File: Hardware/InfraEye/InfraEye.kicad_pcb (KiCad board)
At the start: 2 copper layers, 11 parts, among them Q1 Q_NPN_BCE, U1 MLX90640, U2 ESP32-WROOM-32, U3 TFT_SPI_24_LCD, U4 MLX90640

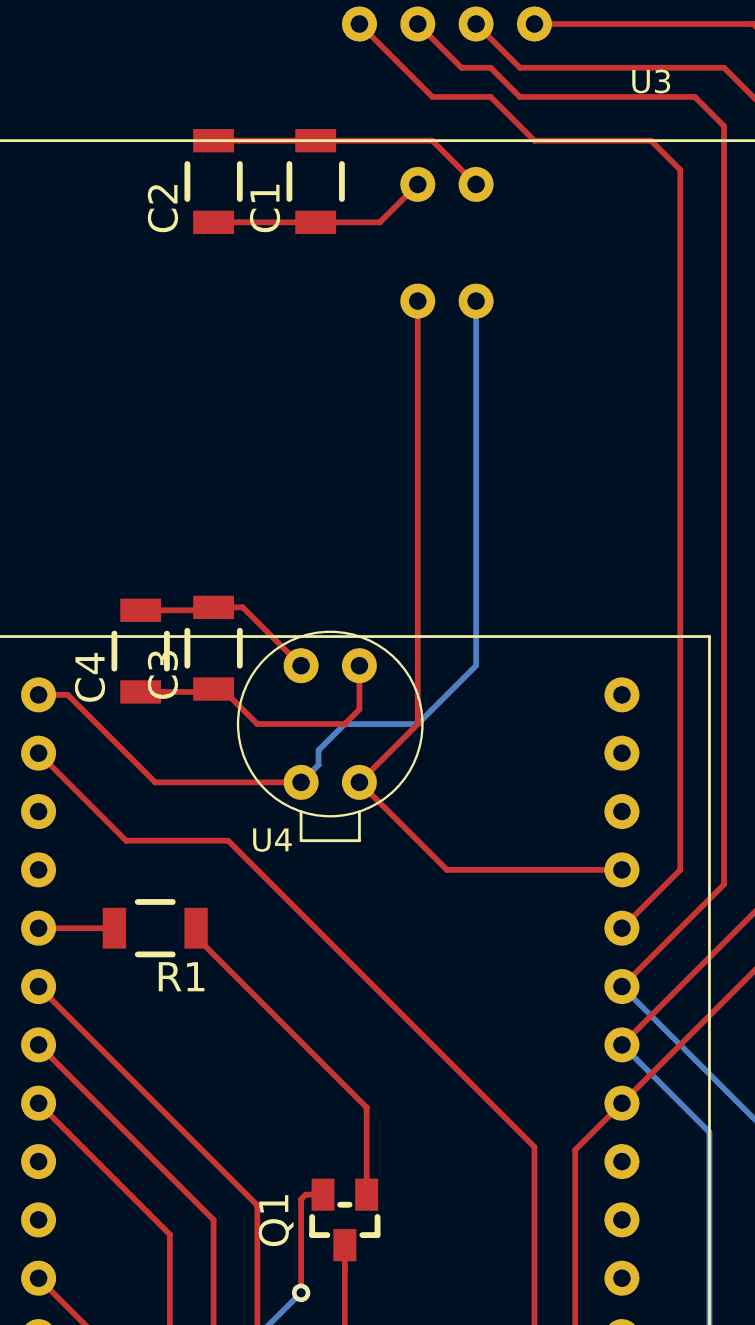
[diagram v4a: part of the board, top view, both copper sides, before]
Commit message: Updated PCB - added text, finished track routing and fill areas. After verifying that it works as it is on schematics, it will be sent out for review.
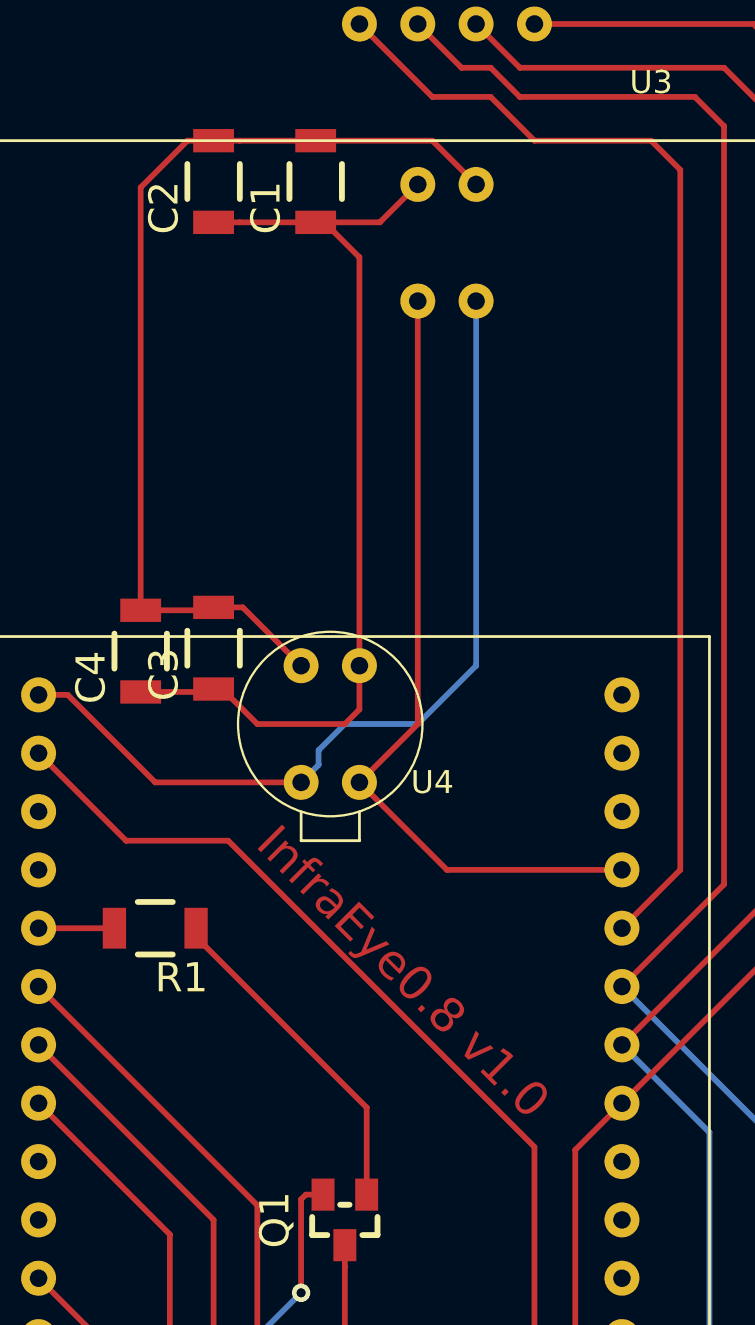
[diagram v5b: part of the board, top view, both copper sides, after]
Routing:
- net GND: track 32.0 -> 54.5 mm
- net +3V3: track 50.6 -> 70.9 mm
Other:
- board text added: "InfraEye0.8 v1.0"
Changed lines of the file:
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@@
   (general
     (thickness 1.6)
-    (drawings 2)
-    (tracks 117)
+    (drawings 3)
+    (tracks 123)
     (zones 0)
     (modules 11)
@@
   (module InfraEye:MLX90614 (layer F.Cu)
     (at 124.46 76.2 180)
-    (fp_text reference U4 (at 3.81 -2.54) (layer F.SilkS)
+    (fp_text reference U4 (at -3.175 0) (layer F.SilkS)
       (effects (font (size 1 1) (thickness 0.15)))
     )
-    (fp_text value MLX90640 (at 1.27 -3.81) (layer F.Fab)
+    (fp_text value MLX90640 (at -4.445 -1.905) (layer F.Fab)
       (effects (font (size 1 1) (thickness 0.15)))
     )
@@
     )
   )
+  (gr_text "InfraEye0.8 v1.0" (at 126.365 84.455 315) (layer F.Cu)
+    (effects (font (size 1.5 1.5) (thickness 0.3)))
+  )
   (gr_line (start 139.7 69.85) (end 139.7 118.11) (layer F.SilkS) (width 0.12))
   (gr_line (start 106.68 69.85) (end 139.7 69.85) (layer F.SilkS) (width 0.12))
-  (via (at 121.92 98.425) (size 0.8) (drill 0.4) (layers F.Cu B.Cu) (net 29))
   (segment (start 128.27 80.01) (end 135.89 80.01) (width 0.25) (layer F.Cu) (net 1))
   (segment (start 124.46 76.2) (end 128.27 80.01) (width 0.25) (layer F.Cu) (net 1))
@@
   (segment (start 127.635 48.26) (end 129.54 50.165) (width 0.25) (layer F.Cu) (net 2))
   (segment (start 122.555 48.26) (end 127.635 48.26) (width 0.25) (layer F.Cu) (net 2))
+  (segment (start 116.971 48.26) (end 114.935 50.296) (width 0.25) (layer F.Cu) (net 2))
+  (segment (start 118.11 48.26) (end 116.971 48.26) (width 0.25) (layer F.Cu) (net 2))
+  (segment (start 114.935 50.296) (end 114.935 68.707) (width 0.25) (layer F.Cu) (net 2))
   (segment (start 121.92 76.2) (end 115.57 76.2) (width 0.25) (layer F.Cu) (net 3))
   (segment (start 111.76 72.39) (end 110.49 72.39) (width 0.25) (layer F.Cu) (net 3))
@@
   (segment (start 116.205 95.885) (end 110.49 90.17) (width 0.25) (layer F.Cu) (net 28))
   (segment (start 116.205 107.315) (end 116.205 95.885) (width 0.25) (layer F.Cu) (net 28))
+  (via (at 121.92 98.425) (size 0.8) (drill 0.4) (layers F.Cu B.Cu) (net 29))
   (segment (start 117.983 72.263) (end 118.11 72.136) (width 0.25) (layer F.Cu) (net 29))
   (segment (start 114.935 72.263) (end 117.983 72.263) (width 0.25) (layer F.Cu) (net 29))
@@
   (segment (start 110.49 107.95) (end 112.395 107.95) (width 0.25) (layer B.Cu) (net 29))
   (segment (start 112.395 107.95) (end 121.92 98.425) (width 0.25) (layer B.Cu) (net 29))
+  (segment (start 122.936 51.816) (end 122.555 51.816) (width 0.25) (layer F.Cu) (net 29))
+  (segment (start 124.46 53.34) (end 122.936 51.816) (width 0.25) (layer F.Cu) (net 29))
+  (segment (start 124.46 71.12) (end 124.46 53.34) (width 0.25) (layer F.Cu) (net 29))
   (segment (start 129.54 114.49237) (end 129.54 115.57) (width 0.25) (layer F.Cu) (net 30))
   (segment (start 129.54 109.347) (end 129.54 114.49237) (width 0.25) (layer F.Cu) (net 30))

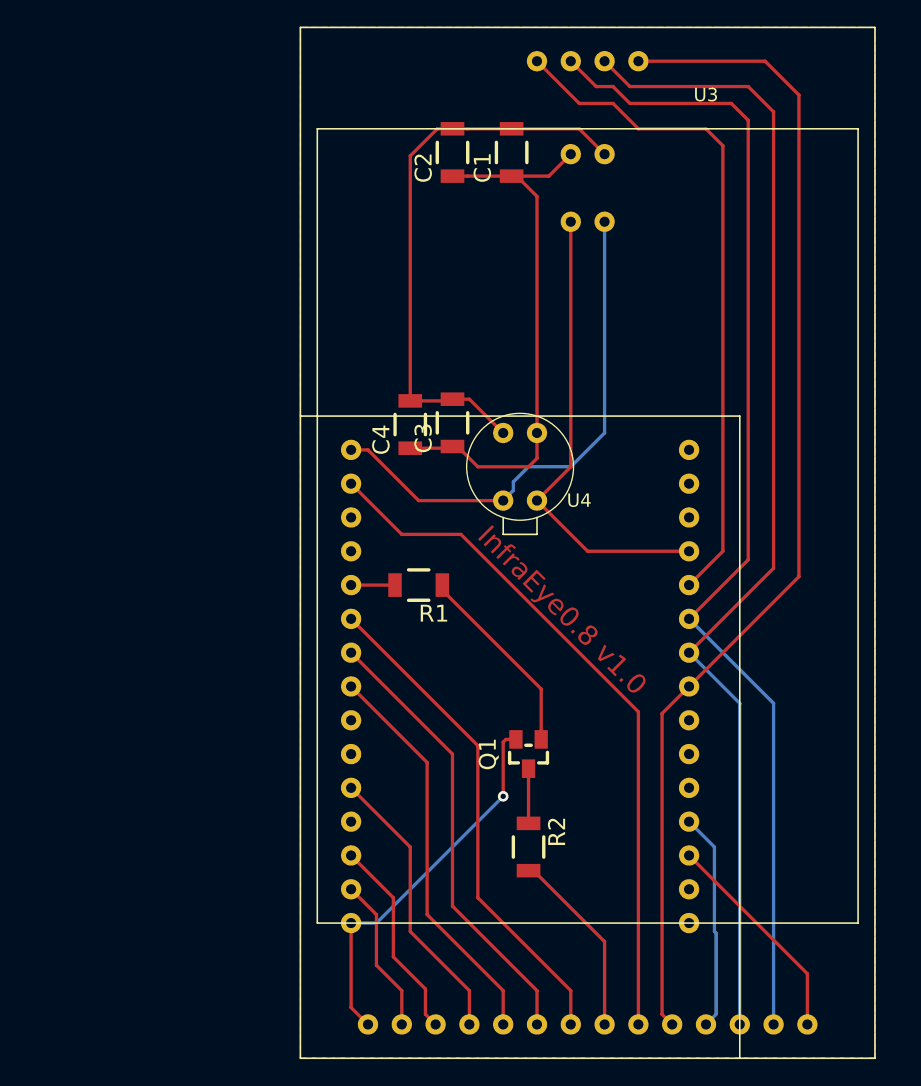
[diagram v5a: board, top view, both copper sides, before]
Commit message: Swapped I2C lines for better trace routing Further improvemets to board, added holes for easier board separation.
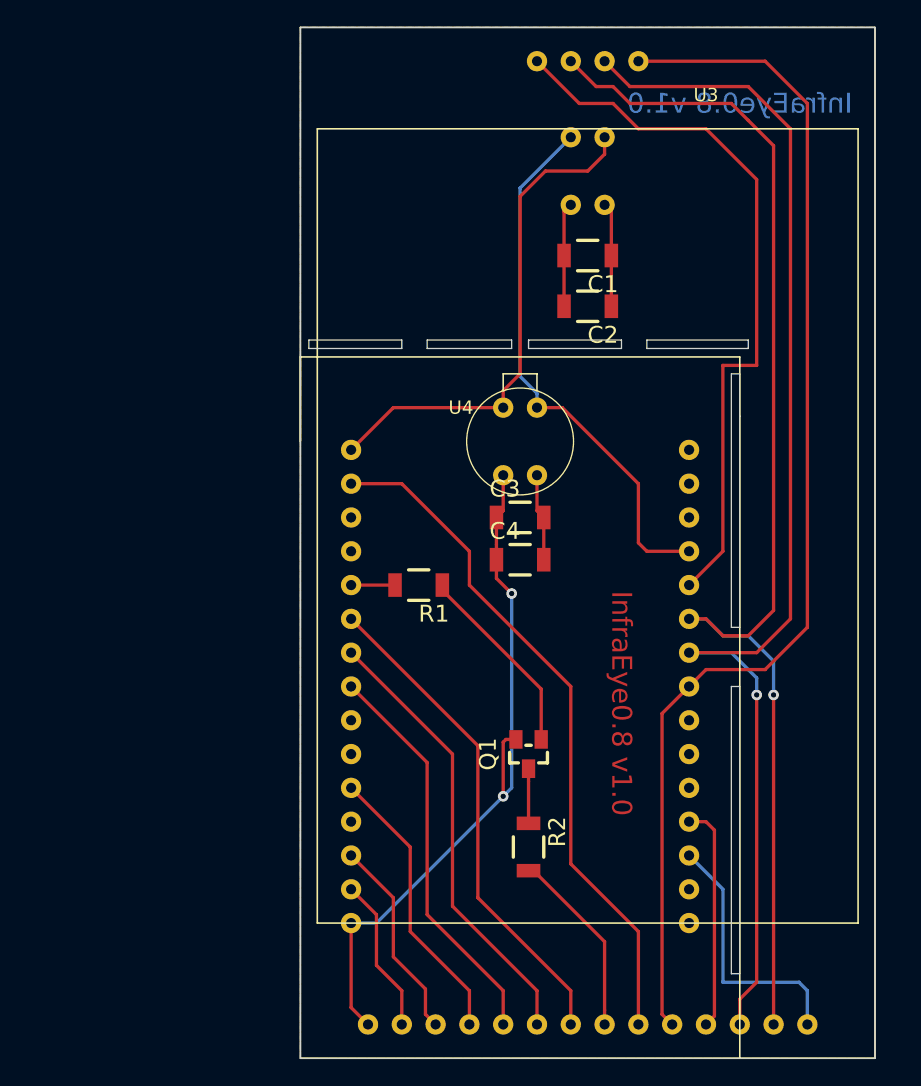
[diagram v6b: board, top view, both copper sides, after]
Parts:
- moved C2 15.4 mm to (128.3, 61.6), turned to 180 degrees
- moved C4 13.1 mm to (123.2, 80.6), turned to 0 degrees
- moved C1 9.63 mm to (128.3, 57.8), turned to 180 degrees
- moved C3 8.74 mm to (123.2, 77.5), turned to 0 degrees
- moved U4 7.43 mm to (121.9, 69.2), turned to 0 degrees
- moved U1 6.84 mm to (129.5, 48.9), turned to 180 degrees
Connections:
- U2 pad 12: Net-(U1-Pad1) -> Net-(U1-Pad4)
- U2 pad 30: Net-(U1-Pad4) -> Net-(U1-Pad1)
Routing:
- net GND: track 54.5 -> 26.1 mm
- net +3V3: track 70.9 -> 61.5 mm, vias 1 -> 2
- net Net-(U2-Pad10): track 87.6 -> 95.4 mm, vias 0 -> 1
- net Net-(U2-Pad9): track 87.1 -> 94.0 mm, vias 0 -> 1
- net Net-(U2-Pad11): track 51.3 -> 54.9 mm
- net Net-(U2-Pad3): track 16.4 -> 19.7 mm
- net Net-(U2-Pad8): track 87.5 -> 90.7 mm
- net Net-(U1-Pad1): track 35.0 -> 38.1 mm
- net Net-(U1-Pad4): track 39.0 -> 40.9 mm
- net Net-(U2-Pad4): track 16.4 -> 17.0 mm
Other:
- board outline added: 43.2 x 77.5 mm

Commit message: AC power supply added also to PCB
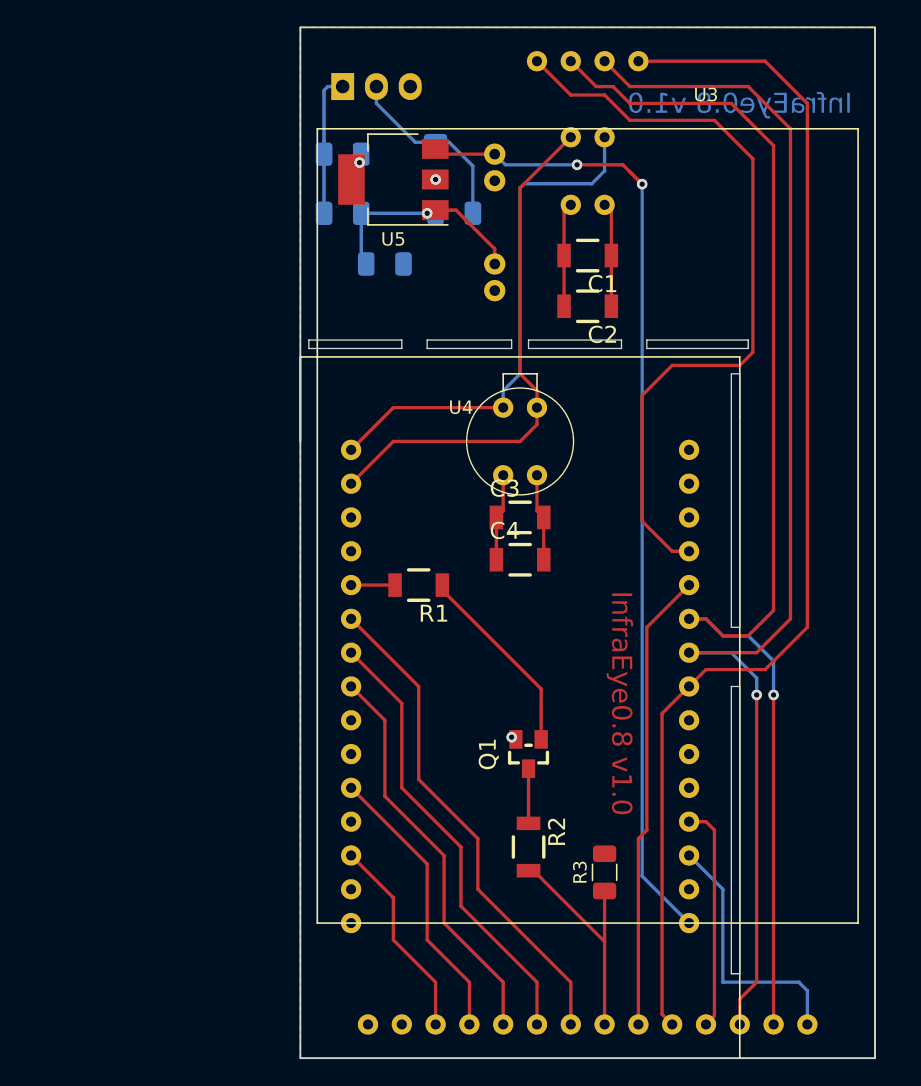
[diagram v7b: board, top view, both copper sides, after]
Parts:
- added C5: CP, Capacitor_THT:C_Radial_D5.0mm_H11.0mm_P2.00mm, B.Cu at (121.3, 58.4)
- added C6: CP, Capacitor_THT:C_Radial_D5.0mm_H11.0mm_P2.00mm, B.Cu at (121.3, 50.2)
- added D1: D, Diode_SMD:D_1206_3216Metric, B.Cu at (109.9, 54.6)
- added D2: D, Diode_SMD:D_1206_3216Metric, B.Cu at (118.2, 54.6)
- added D3: D, Diode_SMD:D_1206_3216Metric, B.Cu at (109.9, 50.2)
- added D4: D, Diode_SMD:D_1206_3216Metric, B.Cu at (116.8, 50.7)
- added D5: D_Zener, Diode_SMD:D_1206_3216Metric, B.Cu at (113.0, 58.4)
- added J1: Conn_01x03_Male, Connector:FanPinHeader_1x03_P2.54mm_Vertical, B.Cu at (109.9, 45.1)
- added R3: R, Resistor_SMD:R_1206_3216Metric, F.Cu at (129.5, 104.1)
- added U5: LT1129-3.3_SOT223, Package_TO_SOT_SMD:SOT-223-3_TabPin2, F.Cu at (113.7, 52.1)
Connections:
- U2 pad 1: Net-(U2-Pad1) -> +5V
- U2 pad 12: Net-(U1-Pad4) -> Net-(U2-Pad12)
- U2 pad 29: Net-(U2-Pad29) -> Net-(U1-Pad4)
- U3 pad 15: Net-(U2-Pad11) -> Net-(U2-Pad12)
- U3 pad 9: Net-(U2-Pad29) -> Net-(U2-Pad11)
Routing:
- net +5V: track 0.00 -> 74.6 mm, vias 0 -> 2
- net Net-(U2-Pad12): track 0.00 -> 58.0 mm
- net Net-(U2-Pad29): track 51.8 -> 0.00 mm
- net +3V3: track 61.5 -> 14.4 mm, vias 2 -> 1
- net Net-(U2-Pad11): track 54.9 -> 34.6 mm
- net Net-(C5-Pad1): track 0.00 -> 15.7 mm, vias 0 -> 1
- net Net-(D2-Pad1): track 0.00 -> 14.0 mm
- net GND: track 26.1 -> 14.4 mm, vias 0 -> 2
- net Net-(D1-Pad2): track 0.00 -> 10.8 mm
- net Net-(R2-Pad2): track 14.1 -> 18.0 mm
- net Net-(U1-Pad4): track 40.9 -> 39.5 mm
- net Net-(U1-Pad1): track 38.1 -> 39.2 mm
